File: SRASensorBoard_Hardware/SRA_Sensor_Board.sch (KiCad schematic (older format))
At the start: 63 parts

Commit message: Started PCb and Made changes to schematic
Updated schematic with annotated parts, associated footprints for each part, and by generating a netlist.

Updated PCB by including all major components on the board and some minor.
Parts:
- C1, C10, C11, C2, C3, C8, C9: renamed from C?; footprint (none) -> Capacitor_SMD:C_0603_1608Metric_Pad1.05x0.95mm_HandSolder
- C4, C5, C6, C7: renamed from C?; value 10u -> 10uF; footprint (none) -> Capacitor_SMD:C_0603_1608Metric_Pad1.05x0.95mm_HandSolder
- Conn1: footprint (none) -> MRDT_Connectors:MOLEX_SL_04_Vertical
- Conn2: renamed from Conn?; footprint (none) -> MRDT_Connectors:Anderson_2_Horizontal_Side_by_Side
- Conn3: renamed from Conn?; footprint (none) -> MRDT_Connectors:MOLEX_SL_04_Vertical
- Conn4: renamed from Conn?; footprint (none) -> MRDT_Connectors:MOLEX_SL_05_Vertical
- Conn5: renamed from Conn?; footprint (none) -> MRDT_Connectors:MOLEX_SL_02_Vertical
- D1, D10, D11, D12, D13, D14, D2, D3, D4, D5, D6, D7, D8, D9: renamed from D?; footprint (none) -> Diode_SMD:D_0603_1608Metric_Pad1.05x0.95mm_HandSolder
- L1: renamed from L?; footprint (none) -> Inductor_SMD:L_0603_1608Metric_Pad1.05x0.95mm_HandSolder
- R1, R10, R11, R12, R13, R14, R15, R16, R17, R18, R19, R2, R20, R3, R4, R5, R6, R7, R8, R9: renamed from R?; footprint (none) -> Resistor_SMD:R_0603_1608Metric_Pad1.05x0.95mm_HandSolder
- U1: renamed from U?; footprint (none) -> MRDT_ICs:TPS55340
- U2, U3: renamed from U?; footprint (none) -> MRDT_Devices:OKI_Horizontal
- U4: renamed from U?; footprint (none) -> MRDT_Shields:TM4C129E_Launchpad_X9_THT_BOTTOM; symbol MRDT_Shields:TM4C129E_Launchpad -> SRA_Sensor_Board-rescue:TM4C129E_Launchpad-MRDT_Shields

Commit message: Added some footprints and other stuff I honeslty forgot
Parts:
- removed C1: 10uF, Capacitor_SMD:C_0603_1608Metric_Pad1.05x0.95mm_HandSolder, symbol Device:C
- removed C11: 1uF, Capacitor_SMD:C_0603_1608Metric_Pad1.05x0.95mm_HandSolder, symbol Device:C
- removed D1: 700mV 3A, Diode_SMD:D_0603_1608Metric_Pad1.05x0.95mm_HandSolder, symbol Device:D_Zener
- removed L1: 15uH, Inductor_SMD:L_0603_1608Metric_Pad1.05x0.95mm_HandSolder, symbol pspice:INDUCTOR
- removed U1: TPS55340, MRDT_ICs:TPS55340, symbol MRDT_ICs:TPS55340
- added C1: 120uF, Capacitor_SMD:C_0603_1608Metric_Pad1.05x0.95mm_HandSolder, symbol Device:CP1
- added C11: 82uF, Capacitor_SMD:C_0603_1608Metric_Pad1.05x0.95mm_HandSolder, symbol Device:CP1
- added D1: 950mV 10A, Diode_THT:D_5W_P5.08mm_Vertical_KathodeUp, symbol Device:D_Schottky
- added D15: LED, Diode_SMD:D_0603_1608Metric_Pad1.05x0.95mm_HandSolder, symbol Device:LED
- added L1: 4.7uH 11.2mOhm, SRA_Hardware:Donald_Shaw_SRP1270, symbol Device:L
- added Q1: CSD17305Q5A, Package_TO_SOT_SMD:TDSON-8-1, symbol Transistor_FET:CSD17305Q5A
- added R21: 6m, Resistor_SMD:R_0603_1608Metric_Pad1.05x0.95mm_HandSolder, symbol Device:R
- added R22: 1000, Resistor_SMD:R_0603_1608Metric_Pad1.05x0.95mm_HandSolder, symbol Device:R
- added SW1: Relay_SPST, symbol MRDT_Switches:Relay_SPST
- added U1: LM3478MMX_NOPB, SRA_Hardware:LM3478MMX&slash_NOPB, symbol 2019-10-10_22-50-45:LM3478MMX_NOPB
- C10: value 10uF -> 82uF
- C3: value 33nF -> 10pF
- C8: value 150nF -> 1nF
- C9: value 2.7nF -> 22nF
- R1: value 1000 -> 18.2k
- R2: value 953 -> 3.48k
- R3: value 60.4k -> 18.2k
- R4: value 169k -> 100
- R5: value 10k -> 26.7k
- U4: footprint MRDT_Shields:TM4C129E_Launchpad_X9_THT_BOTTOM -> MRDT_Shields:TM4C129E_Launchpad_X7_THT_TOP
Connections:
- net labels added: Buck_Turnon
- wire segments 149 -> 152
- no-connect marks 67 -> 66

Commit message: Killed old sensors added new sensors
Added usb support to the io pins.
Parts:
- removed Conn1: Temp/Humid, MRDT_Connectors:MOLEX_SL_04_Vertical, symbol MRDT_Connectors:Molex_SL_04
- removed Conn3: Methane, MRDT_Connectors:MOLEX_SL_04_Vertical, symbol MRDT_Connectors:Molex_SL_04
- removed R6, R7: 10K, Resistor_SMD:R_0603_1608Metric_Pad1.05x0.95mm_HandSolder, symbol Device:R
- removed U4: TM4C129E_Launchpad, MRDT_Shields:TM4C129E_Launchpad_X7_THT_TOP, symbol SRA_Sensor_Board-rescue:TM4C129E_Launchpad-MRDT_Shields
- added C12, C13, C14: 1uF, Capacitor_SMD:C_0603_1608Metric_Pad1.05x0.95mm_HandSolder, symbol Device:C
- added J1: USB_B_Micro, Connector_USB:USB_Micro-B_Molex-105017-0001, symbol Connector:USB_B_Micro
- added U4: TM4C129E_Launchpad, MRDT_Shields:TM4C129E_Launchpad_FULL_THT_TOP, symbol MRDT_Shields:TM4C129E_Launchpad
- added U5: MAX232, footprints:MAX232DR, symbol Interface_UART:MAX232
- U1: symbol 2019-10-10_22-50-45:LM3478MMX_NOPB -> SRA_Sensor_Board-rescue:LM3478MMX_NOPB-2019-10-10_22-50-45
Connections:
- net labels added: USB_Data_1, USB_Data_2, USB_TIVA_1, USB_TIVA_2
- net labels removed: Methane_Data, Temp_Humid_Data
- wire segments 152 -> 153
- no-connect marks 66 -> 64
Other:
- note removed: "101020055"
- note removed: "DHT22"
- moved on the sheet: Conn4, Conn5

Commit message: Added sensors and cleaned repo
Added Flow sensor
Added C02 sensor
Removed relay replaced with power mosfet
Added resistor to the uv LED
Deleted projects that were not a part of the repo
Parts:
- removed SW1: Relay_SPST, symbol MRDT_Switches:Relay_SPST
- added Conn1, Conn3: Molex_SL_04, MRDT_Connectors:MOLEX_SL_04_Vertical, symbol MRDT_Connectors:Molex_SL_04
- added D16, D17, D18: LED, Diode_SMD:D_0603_1608Metric_Pad1.05x0.95mm_HandSolder, symbol Device:LED
- added R23, R24, R7: 500, Resistor_SMD:R_0603_1608Metric_Pad1.05x0.95mm_HandSolder, symbol Device:R
- added R6: 3.33, Resistor_SMD:R_0603_1608Metric_Pad1.05x0.95mm_HandSolder, symbol Device:R
- added U6: IRF7821PbF, footprints:IRF7821PBF, symbol MRDT_ICs:IRF7821PbF
- U4: symbol MRDT_Shields:TM4C129E_Launchpad -> SRA_Sensor_Board-rescue:TM4C129E_Launchpad-MRDT_Shields
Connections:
- net labels added: C02_In, C02_Out, Flow_Output, Flow_Receive
- net labels removed: Buck_Turnon
- wire segments 153 -> 180
- no-connect marks 64 -> 58
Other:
- note added: "Flow_Sensor"
- note added: "Indicators"
- note added: "NGM_1"
- note added: "T6613_CO2_Sensor\n"
- note removed: "Indicator"
- moved on the sheet: C1, C10, C11, C12, C13, C14, C2, C3, C8, C9, D1, D10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

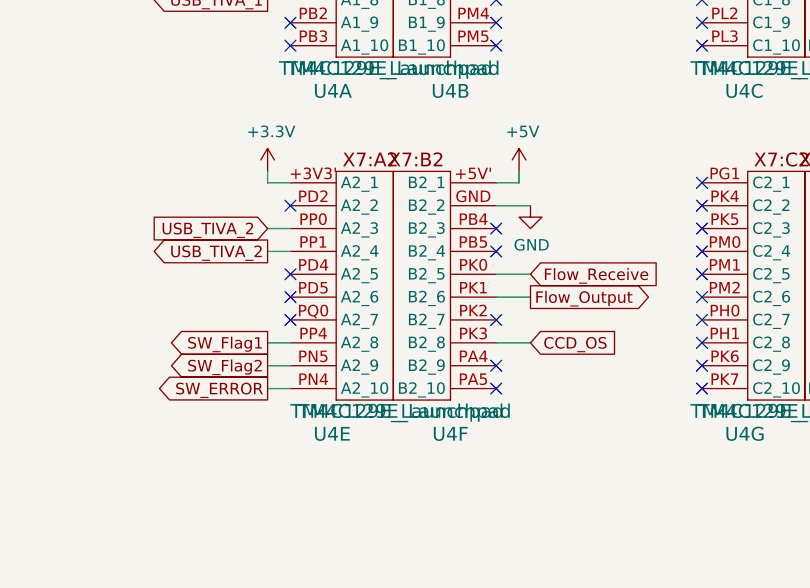
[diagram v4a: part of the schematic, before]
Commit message: Fixed Footprints
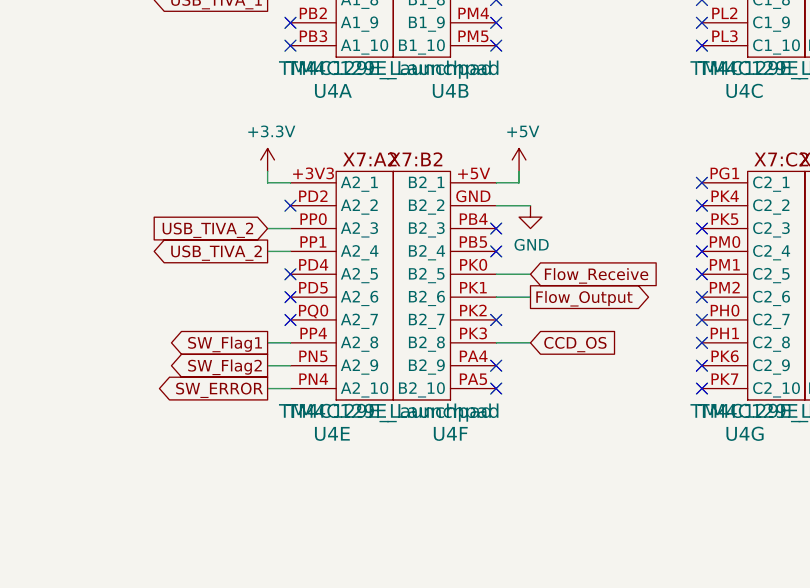
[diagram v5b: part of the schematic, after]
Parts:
- removed unit 5 of U4
- removed unit 6 of U4
- added unit 5 of U4
- added unit 6 of U4
- L1: footprint SRA_Hardware:Donald_Shaw_SRP1270 -> custom:Donald_Shaw_SRP1270
- U1: footprint SRA_Hardware:LM3478MMX&slash_NOPB -> custom:LM3478MMX&slash_NOPB
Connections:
- net +3V3: now also U4.+3V3 (A2_1)
- net +5V: now also U4.+5V (B2_1)
- net CCD_OS: now also U4.PK3 (B2_8)
- net Flow_Output: now also U4.PK1 (B2_6)
- net Flow_Receive: now also U4.PK0 (B2_5)
- net GND: now also U4.GND (B2_2)
- net SW_ERROR: now also U4.PN4 (A2_10)
- net SW_Flag1: now also U4.PP4 (A2_8)
- net SW_Flag2: now also U4.PN5 (A2_9)
- net USB_TIVA_2: now also U4.PP0 (A2_3), U4.PP1 (A2_4)

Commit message: Changes to board
LED area is currently being made. Slight changes to wiring. Added schematic for SMD diode. Overall structure is the same.
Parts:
- removed D1: 950mV 10A, Diode_THT:D_5W_P5.08mm_Vertical_KathodeUp, symbol Device:D_Schottky
- added D1: SBRD10200TR, MRDT_ICs:SMC_DPAK, symbol SBRD10200TR:SBRD10200TR
- U4: symbol SRA_Sensor_Board-rescue:TM4C129E_Launchpad-MRDT_Shields -> SRA_Sensor_Board-rescue:TM4C129E_Launchpad-MRDT_Shields-SRA_Sensor_Board-rescue
- U4: symbol MRDT_Shields:TM4C129E_Launchpad -> SRA_Sensor_Board-rescue:TM4C129E_Launchpad-MRDT_Shields-SRA_Sensor_Board-rescue
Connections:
- net +24V: now also D1.3 (BASE_CATHODE)
- net +3V3: now also U4.+3V3' (A2_1); no longer U4.+3V3 (A2_1)
- net +5V: now also U4.+5V' (B2_1); no longer U4.+5V (B2_1)
- net at L1.2, Q1.5 (D): now also D1.1 (ANODE_1), D1.2 (ANODE_2)
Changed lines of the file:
@@
 	5950 9350 6100 9350
-Wire Wire Line
-	6100 9350 6100 9700
 Wire Wire Line
 	2550 10050 2250 10050
@@
 Connection ~ 1550 11000
 $Comp
-L Device:D_Schottky D1
-U 1 1 5DAA886E
-P 6350 9700
-F 0 "D1" H 6350 9500 50  0000 C CNN
-F 1 "950mV 10A" H 6350 9600 50  0000 C CNN
-F 2 "Diode_THT:D_5W_P5.08mm_Vertical_KathodeUp" H 6350 9700 50  0001 C CNN
-F 3 "~" H 6350 9700 50  0001 C CNN
-	1    6350 9700
-	-1   0    0    1
-$EndComp
-Wire Wire Line
-	6200 9700 6100 9700
-Connection ~ 6100 9700
-Wire Wire Line
-	6100 9700 6100 9950
-$Comp
 L Device:CP1 C10
 U 1 1 5DAAF9F5
@@
 $EndComp
 Wire Wire Line
-	6700 10650 6700 10400
-Wire Wire Line
 	6700 10400 6550 10400
-Wire Wire Line
-	6700 10400 6700 9700
-Connection ~ 6700 10400
 Wire Wire Line
 	6550 10700 6550 11000
@@
 Wire Wire Line
 	2850 10150 2950 10150
-Wire Wire Line
-	6700 9100 6700 9700
-Wire Wire Line
-	6700 9700 6500 9700
-Wire Wire Line
-	4400 9100 6700 9100
 $Comp
 L Device:R R1
@@
 Wire Wire Line
 	4200 11000 5700 11000
-Connection ~ 6700 9700
 Wire Wire Line
 	6100 11000 6550 11000
@@
 L power:+24V #PWR0106
 U 1 1 5DBA47BF
-P 6700 9100
-F 0 "#PWR0106" H 6700 8950 50  0001 C CNN
-F 1 "+24V" H 6715 9273 50  0000 C CNN
-F 2 "" H 6700 9100 50  0001 C CNN
-F 3 "" H 6700 9100 50  0001 C CNN
-	1    6700 9100
-	1    0    0    -1
-$EndComp
-Connection ~ 6700 9100
+P 7950 9050
+F 0 "#PWR0106" H 7950 8900 50  0001 C CNN
+F 1 "+24V" H 7965 9223 50  0000 C CNN
+F 2 "" H 7950 9050 50  0001 C CNN
+F 3 "" H 7950 9050 50  0001 C CNN
+	1    7950 9050
+	1    0    0    -1
+$EndComp
 $Comp
 L power:GND #PWR0107
@@
 $EndComp
 $Comp
-L SRA_Sensor_Board-rescue:TM4C129E_Launchpad-MRDT_Shields U4
+L SRA_Sensor_Board-rescue:TM4C129E_Launchpad-MRDT_Shields-SRA_Sensor_Board-rescue U4
 U 7 1 5DD2C269
 P 14550 3600
@@
 $EndComp
 $Comp
-L SRA_Sensor_Board-rescue:TM4C129E_Launchpad-MRDT_Shields U4
+L SRA_Sensor_Board-rescue:TM4C129E_Launchpad-MRDT_Shields-SRA_Sensor_Board-rescue U4
 U 8 1 5DD2FD4D
 P 15050 3600
@@
 NoConn ~ 12550 1650
 $Comp
-L SRA_Sensor_Board-rescue:TM4C129E_Launchpad-MRDT_Shields U4
+L SRA_Sensor_Board-rescue:TM4C129E_Launchpad-MRDT_Shields-SRA_Sensor_Board-rescue U4
 U 4 1 5DD10D78
 P 15050 2100
@@
 $EndComp
 $Comp
-L SRA_Sensor_Board-rescue:TM4C129E_Launchpad-MRDT_Shields U4
+L SRA_Sensor_Board-rescue:TM4C129E_Launchpad-MRDT_Shields-SRA_Sensor_Board-rescue U4
 U 3 1 5DD0DE2F
 P 14550 2100
@@
 $EndComp
 $Comp
-L SRA_Sensor_Board-rescue:TM4C129E_Launchpad-MRDT_Shields U4
+L SRA_Sensor_Board-rescue:TM4C129E_Launchpad-MRDT_Shields-SRA_Sensor_Board-rescue U4
 U 2 1 5DCDED37
 P 13250 2100
@@
 $EndComp
 $Comp
-L SRA_Sensor_Board-rescue:TM4C129E_Launchpad-MRDT_Shields U4
+L SRA_Sensor_Board-rescue:TM4C129E_Launchpad-MRDT_Shields-SRA_Sensor_Board-rescue U4
 U 1 1 5DCDAD76
 P 12750 2100
@@
 $EndComp
 $Comp
-L MRDT_Shields:TM4C129E_Launchpad U4
+L SRA_Sensor_Board-rescue:TM4C129E_Launchpad-MRDT_Shields-SRA_Sensor_Board-rescue U4
 U 5 1 5DD95673
 P 12750 3600
@@
 $EndComp
 $Comp
-L MRDT_Shields:TM4C129E_Launchpad U4
+L SRA_Sensor_Board-rescue:TM4C129E_Launchpad-MRDT_Shields-SRA_Sensor_Board-rescue U4
 U 6 1 5DD9982E
 P 13250 3600
@@
 	1    0    0    -1
 $EndComp
+Wire Wire Line
+	7950 9050 7950 9100
+Wire Wire Line
+	7850 9450 7950 9450
+Connection ~ 7950 9450
+$Comp
+L SBRD10200TR:SBRD10200TR D1
+U 1 1 5DDAAED7
+P 6150 9450
+F 0 "D1" H 7000 9715 50  0000 C CNN
+F 1 "SBRD10200TR" H 7000 9624 50  0000 C CNN
+F 2 "MRDT_ICs:SMC_DPAK" H 7700 9550 50  0001 L CNN
+F 3 "http://www.smc-diodes.com/propdf/SBRD10200%20N1314%20REV.A.pdf" H 7700 9450 50  0001 L CNN
+F 4 "SCHOTTKY RECTIFIER" H 7700 9350 50  0001 L CNN "Description"
+F 5 "" H 7700 9250 50  0001 L CNN "Height"
+F 6 "SMC Diode Solutions" H 7700 9150 50  0001 L CNN "Manufacturer_Name"
+F 7 "SBRD10200TR" H 7700 9050 50  0001 L CNN "Manufacturer_Part_Number"
+F 8 "" H 7700 8950 50  0001 L CNN "Mouser Part Number"
+F 9 "" H 7700 8850 50  0001 L CNN "Mouser Price/Stock"
+F 10 "" H 7700 8750 50  0001 L CNN "RS Part Number"
+F 11 "" H 7700 8650 50  0001 L CNN "RS Price/Stock"
+	1    6150 9450
+	1    0    0    -1
+$EndComp
+Wire Wire Line
+	6100 9350 6100 9450
+Wire Wire Line
+	6150 9450 6100 9450
+Connection ~ 6100 9450
+Wire Wire Line
+	6100 9450 6100 9550
+Wire Wire Line
+	6150 9550 6100 9550
+Connection ~ 6100 9550
+Wire Wire Line
+	6100 9550 6100 9950
+Wire Wire Line
+	7950 10400 6700 10400
+Wire Wire Line
+	7950 9450 7950 10400
+Connection ~ 6700 10400
+Wire Wire Line
+	6700 10450 6700 10400
+Wire Wire Line
+	6700 10400 6700 10650
+Wire Wire Line
+	4400 9100 7950 9100
+Connection ~ 7950 9100
+Wire Wire Line
+	7950 9100 7950 9450
 $EndSCHEMATC
